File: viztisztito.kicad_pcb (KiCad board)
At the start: 2 copper layers, 110 x 102 mm, 80 parts, among them J1 CONN_01X01, J2 CONN_01X01, J3 CONN_01X01, J4 CONN_01X01, P1 BOARD_CONN, Q1 BC850, U1 VTX-214-010-205, U2 LTV-847, U3 ACS722, U4 MCP3004, U5 TC77

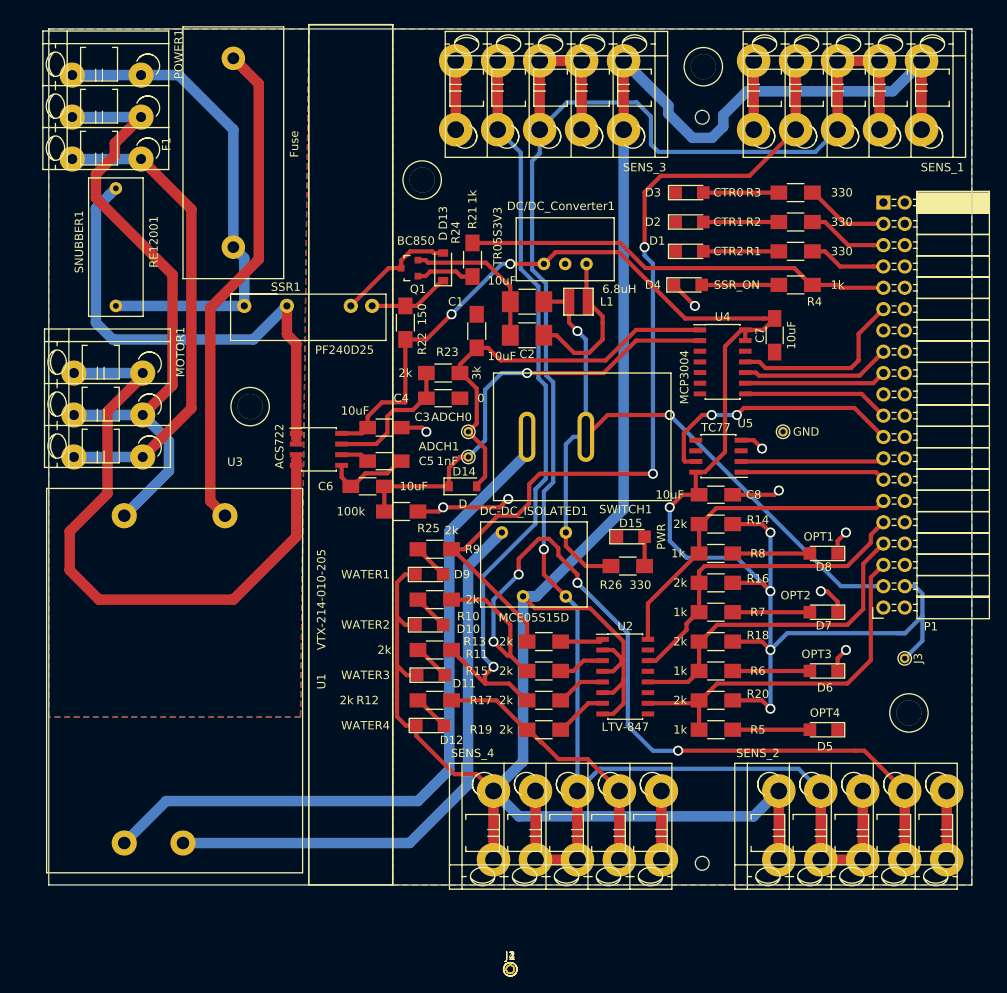
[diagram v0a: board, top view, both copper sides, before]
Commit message: I have fixed the pcb of the 5 connectors
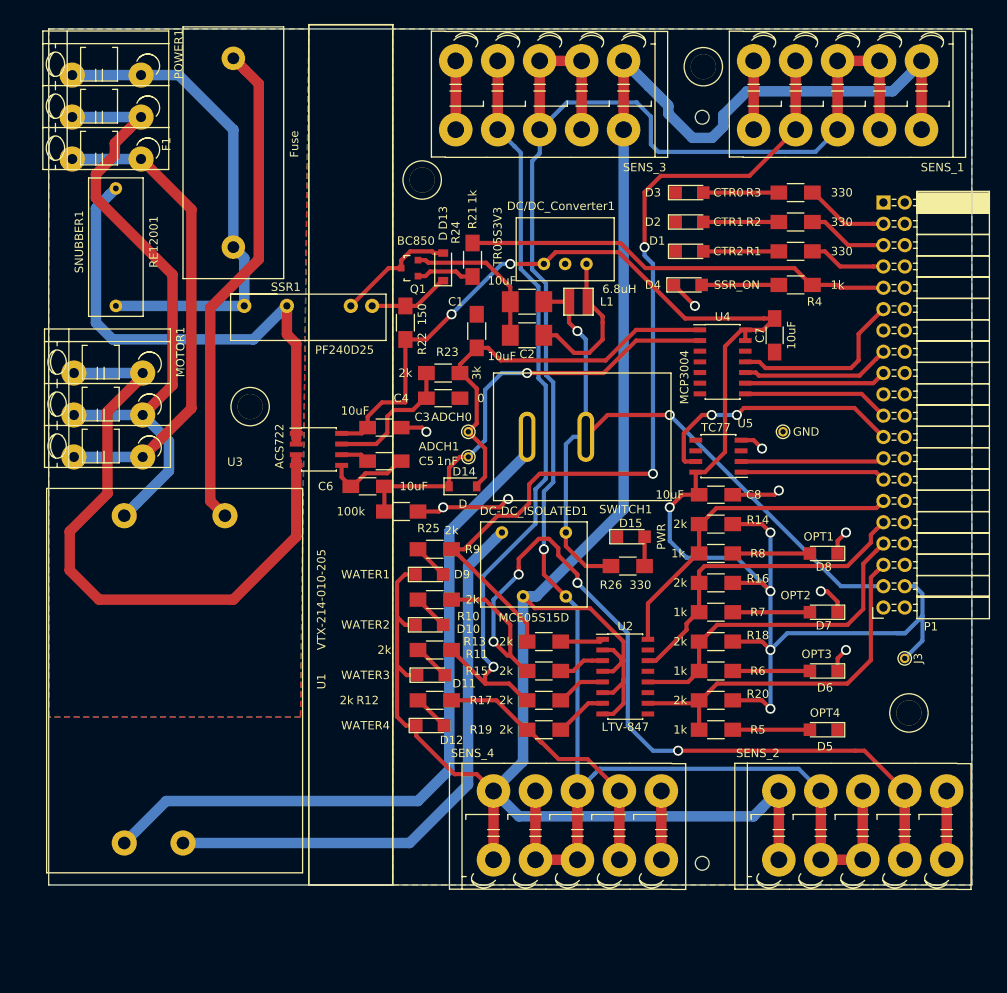
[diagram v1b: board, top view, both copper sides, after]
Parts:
- removed J1, J2, J4: CONN_01X01, Connectors:PINTST

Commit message: I have added the notation of the water level sensors
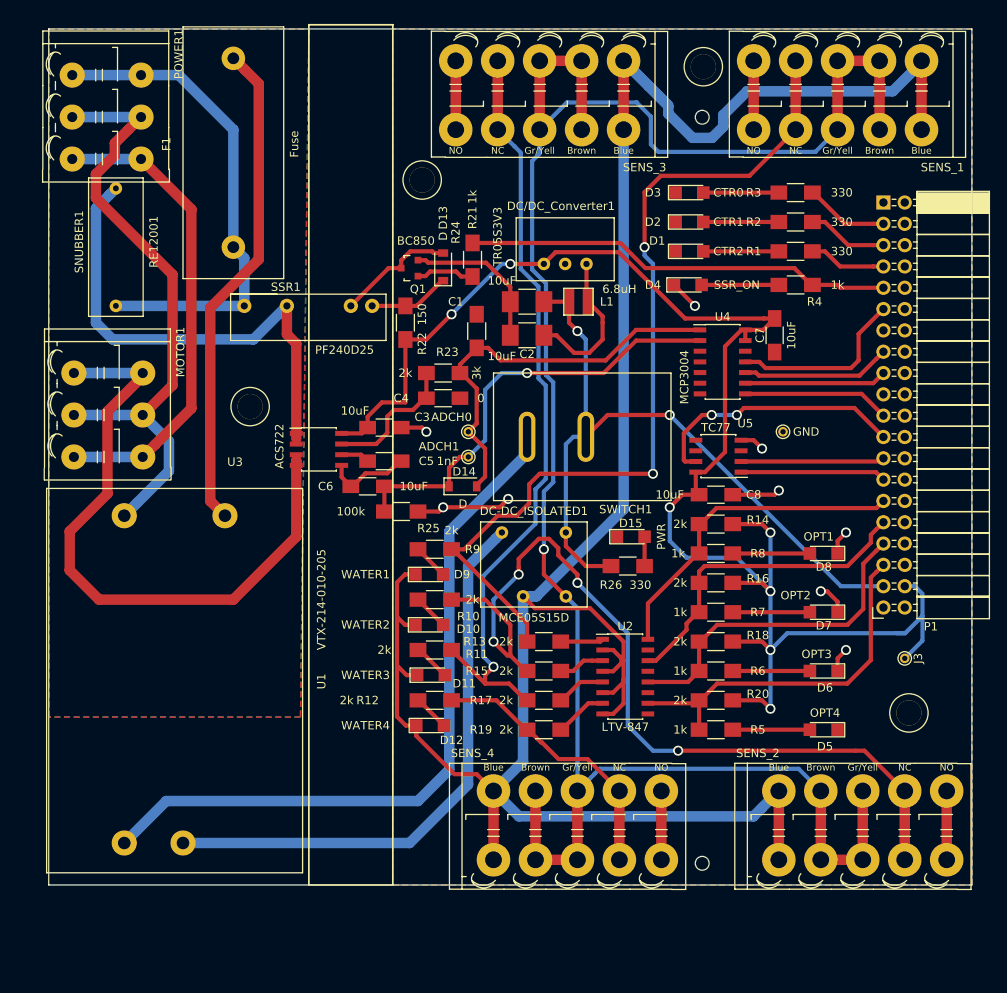
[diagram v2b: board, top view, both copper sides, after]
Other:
- board text added: "Blue"
- board text added: "Brown"
- board text added: "Gr/Yell"
- board text added: "NC"
- board text added: "NO"

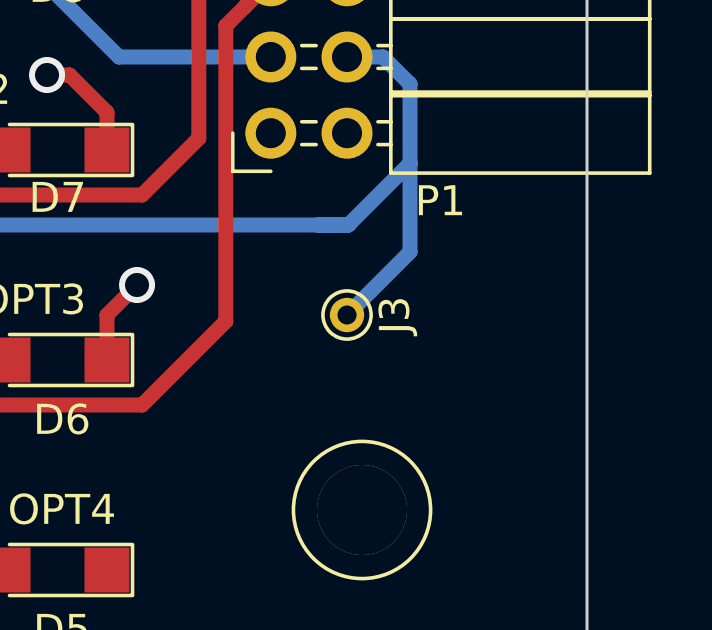
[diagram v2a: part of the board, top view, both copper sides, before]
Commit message: a minor change. The 3.3V pin was not properly annotated
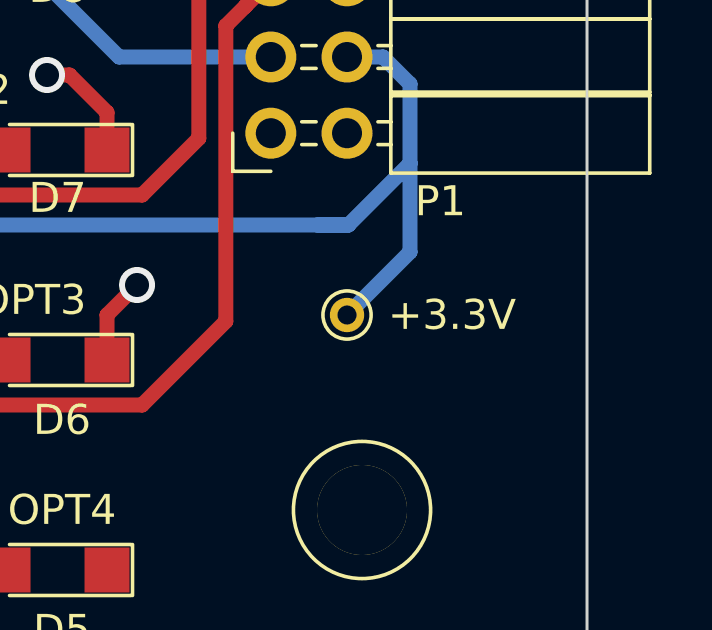
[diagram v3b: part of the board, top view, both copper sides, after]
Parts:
- renumbered J3 to +3.3V
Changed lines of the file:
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@@
     (descr "module 1 pin (ou trou mecanique de percage)")
     (tags DEV)
-    (fp_text reference J3 (at 0 -1.6 270) (layer F.SilkS)
+    (fp_text reference +3.3V (at 0 -3.5 360) (layer F.SilkS)
       (effects (font (size 1 1) (thickness 0.15)))
     )

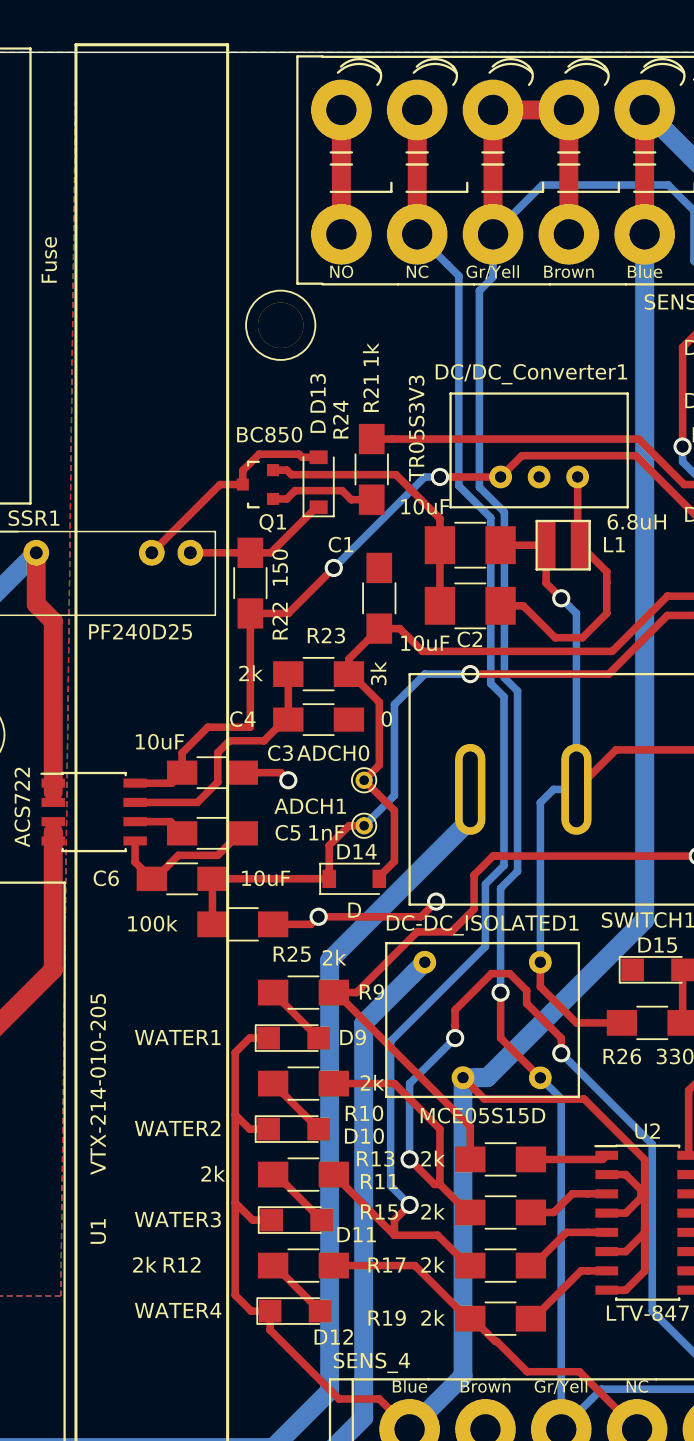
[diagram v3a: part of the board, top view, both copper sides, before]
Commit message: A few more moves + Credit Line
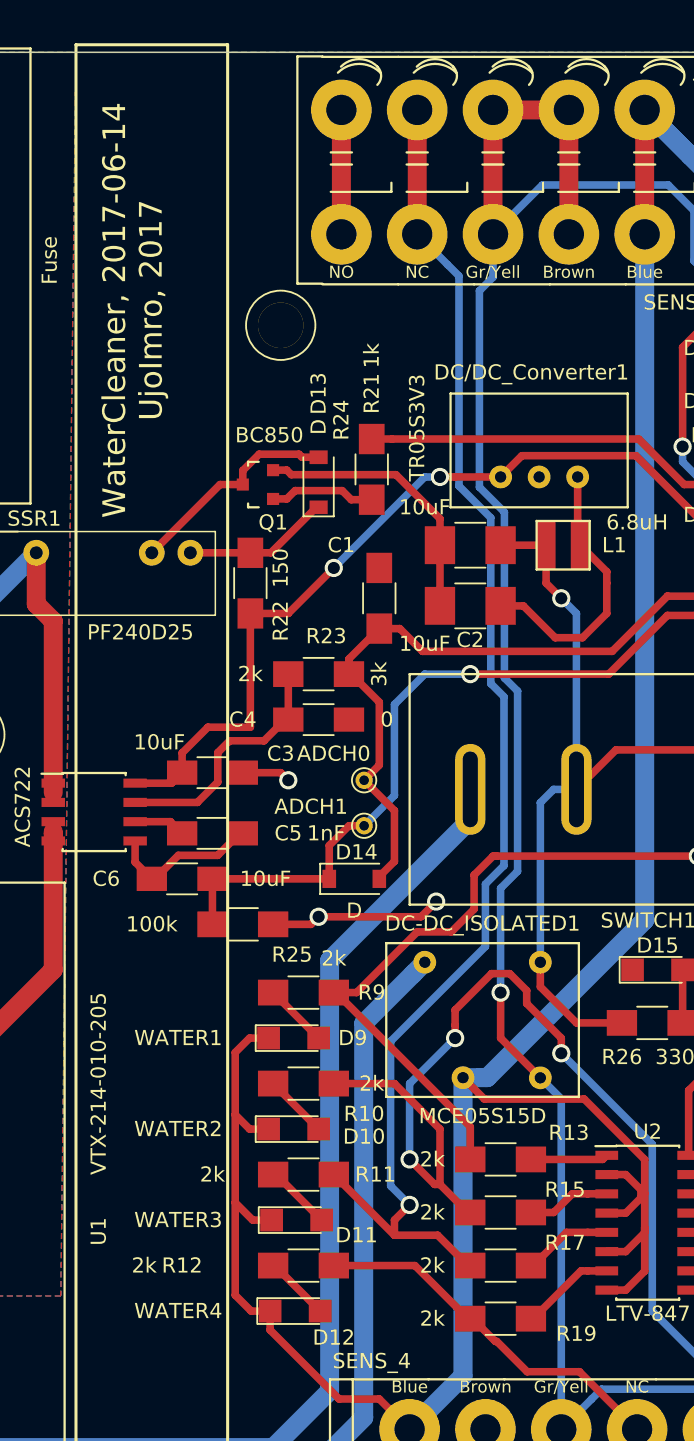
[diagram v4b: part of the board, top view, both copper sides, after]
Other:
- board text added: "WaterCleaner, 2017-06-14 UjoImro, 2017"
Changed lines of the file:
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@@
     (area 23.949999 22.949999 134.050001 125.050001)
     (thickness 1.6)
-    (drawings 28)
+    (drawings 29)
     (tracks 550)
     (zones 0)
@@
     (tags "resistor 1206")
     (attr smd)
-    (fp_text reference R11 (at 5 0.5) (layer F.SilkS)
+    (fp_text reference R11 (at 4.75 0) (layer F.SilkS)
       (effects (font (size 1 1) (thickness 0.15)))
     )
@@
     (tags "resistor 1206")
     (attr smd)
-    (fp_text reference R13 (at 8.25 0 180) (layer F.SilkS)
+    (fp_text reference R13 (at -4.5 1.75 180) (layer F.SilkS)
       (effects (font (size 1 1) (thickness 0.15)))
     )
@@
     (tags "resistor 1206")
     (attr smd)
-    (fp_text reference R15 (at 8 0 180) (layer F.SilkS)
+    (fp_text reference R15 (at -4.25 1.5 180) (layer F.SilkS)
       (effects (font (size 1 1) (thickness 0.15)))
     )
@@
     (tags "resistor 1206")
     (attr smd)
-    (fp_text reference R17 (at 7.5 0 180) (layer F.SilkS)
+    (fp_text reference R17 (at -4.25 1.5 180) (layer F.SilkS)
       (effects (font (size 1 1) (thickness 0.15)))
     )
@@
     (tags "resistor 1206")
     (attr smd)
-    (fp_text reference R19 (at 7.5 0 180) (layer F.SilkS)
+    (fp_text reference R19 (at -5 -1 180) (layer F.SilkS)
       (effects (font (size 1 1) (thickness 0.15)))
     )
@@
       (net 29 /MOTOR+))
   )
+  (gr_text "WaterCleaner, 2017-06-14\nUjoImro, 2017" (at 58.75 40 90) (layer F.SilkS)
+    (effects (font (size 1.5 1.5) (thickness 0.3)))
+  )
   (gr_text NO (at 131 111 360) (layer F.SilkS)

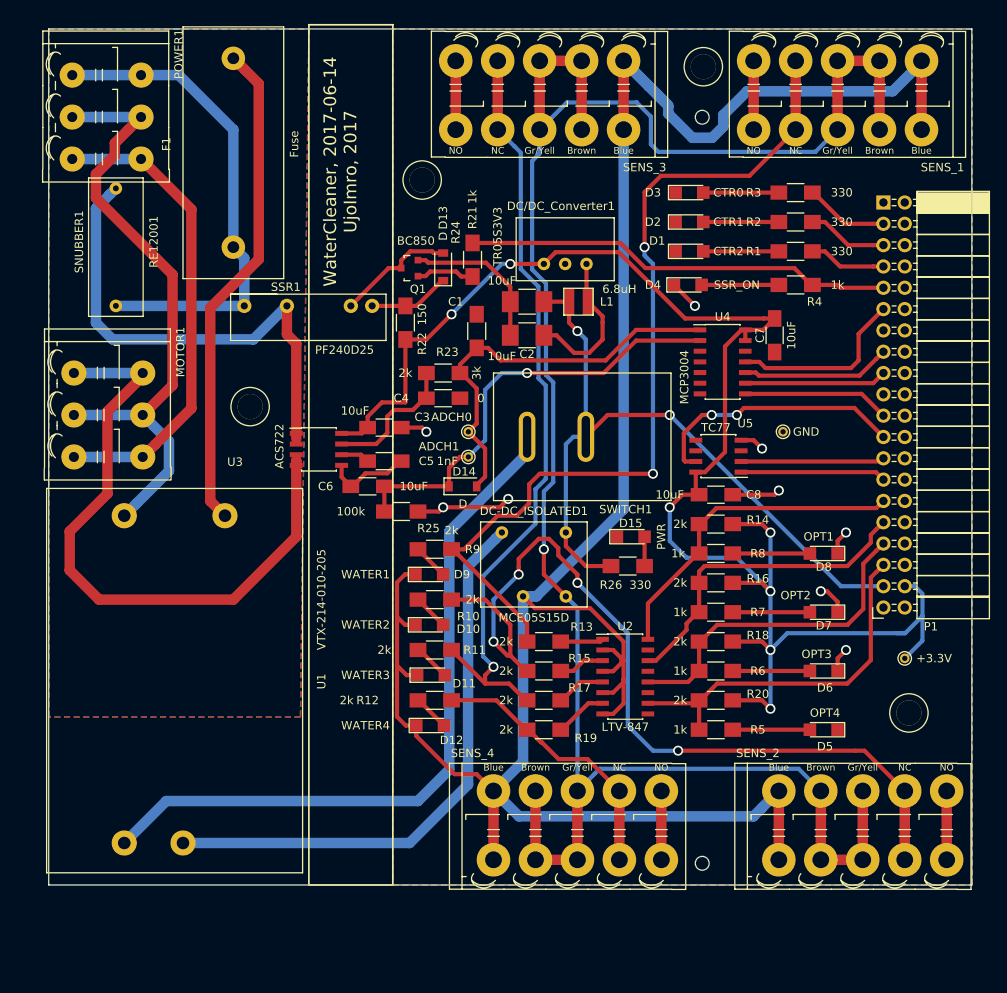
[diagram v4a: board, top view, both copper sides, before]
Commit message: I have fixed the pcb layouts of the parts based on verification of the physical part
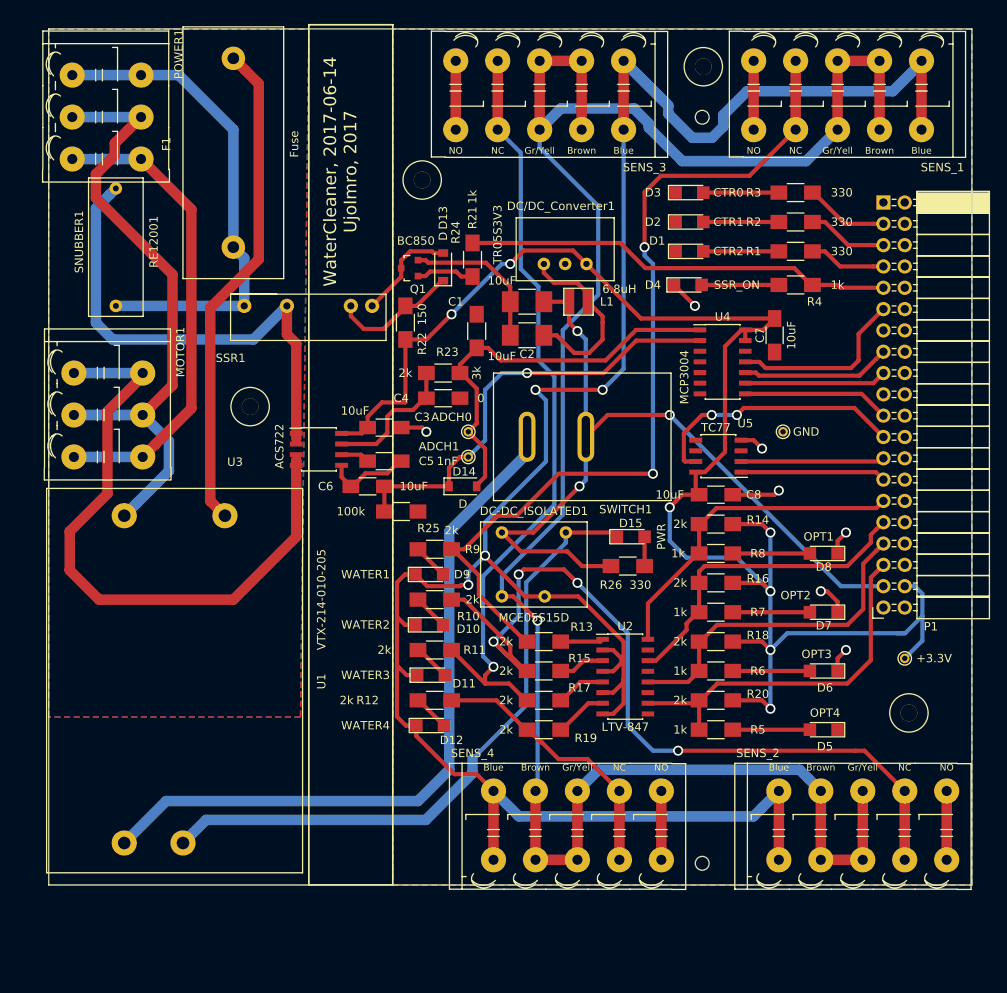
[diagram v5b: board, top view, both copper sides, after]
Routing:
- net +5V: track 86.2 -> 97.3 mm, vias 2 -> 3
- net Net-(D13-Pad1): track 9.70 -> 15.4 mm
- net /water_level/ISOLATED_+15V: track 241.5 -> 246.8 mm
- net Net-(C2-Pad1): track 18.3 -> 22.3 mm
- net GND: track 133.2 -> 130.8 mm, vias 9 -> 7
- net ISOLATED_GND: track 288.7 -> 286.5 mm, vias 0 -> 4
- net Net-(D13-Pad2): track 14.3 -> 12.4 mm
- net Net-(R13-Pad2): track 107.1 -> 105.9 mm
- net Net-(R10-Pad2): track 103.6 -> 102.4 mm
- net Net-(R11-Pad2): track 92.1 -> 92.9 mm

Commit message: final commit before manufacturing
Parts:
- moved SNUBBER1 25.1 mm to (48.8, 70.2), turned to 180 degrees
- moved MOTOR1 16.0 mm to (30.0, 45.5)
- moved REF** 11.7 mm to (38.0, 74.0)
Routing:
- net 230V_GND: track 56.8 -> 16.4 mm
- net Net-(SNUBBER1-Pad1): track 59.5 -> 29.5 mm
- net /MOTOR+: track 77.0 -> 86.3 mm
- net 230V_AC+: track 58.7 -> 67.9 mm
- net 230V_NEUTRAL: track 74.9 -> 72.7 mm
- net /water_level/ISOLATED_+15V: track 246.8 -> 248.1 mm
